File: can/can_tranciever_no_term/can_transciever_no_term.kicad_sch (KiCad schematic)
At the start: 6 parts, among them U5 TCAN3403DRQ1

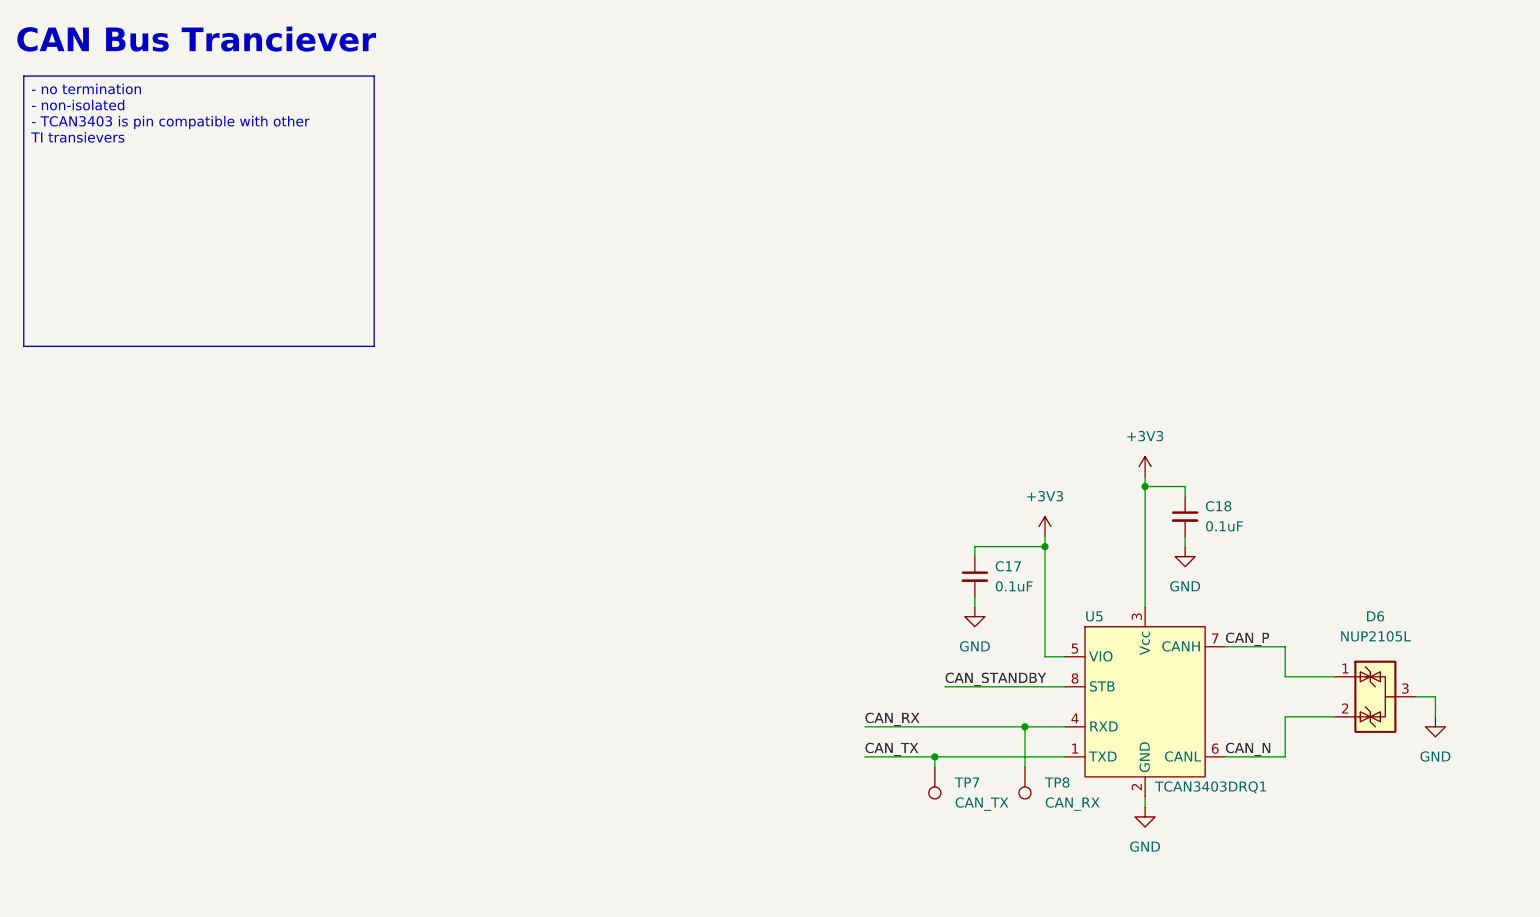
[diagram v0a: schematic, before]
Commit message: added hierarchical labels
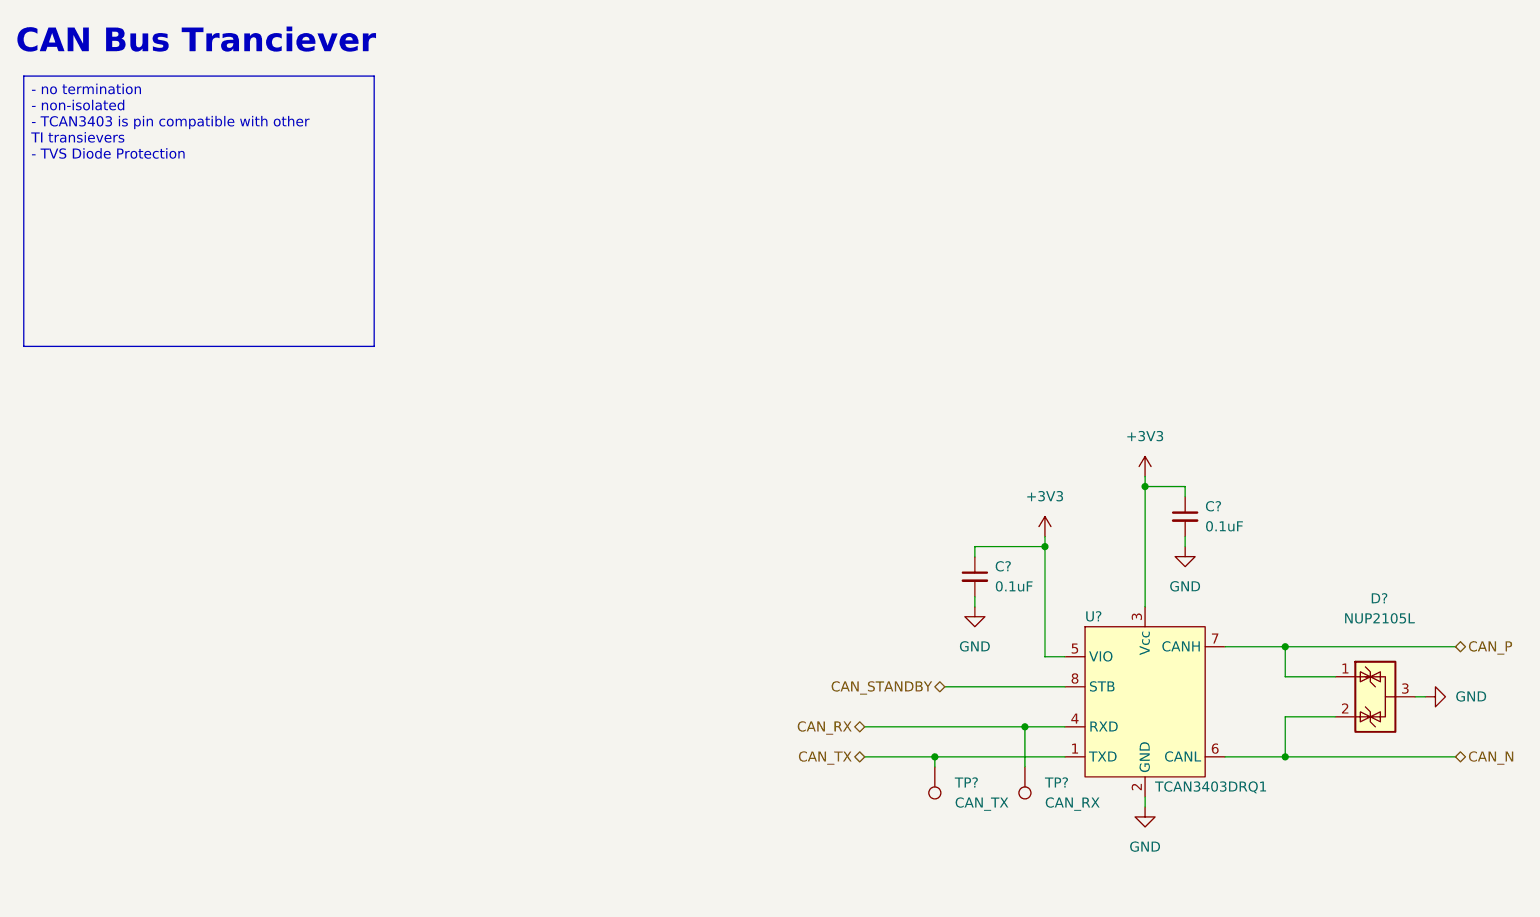
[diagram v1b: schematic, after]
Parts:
- renumbered C17 to C?, C18 to C?, D6 to D?, TP8 to TP?, TP7 to TP?, U5 to U?
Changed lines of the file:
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@@
 		)
 	)
-	(text_box "- no termination\n- non-isolated\n- TCAN3403 is pin compatible with other TI transievers"
+	(text_box "- no termination\n- non-isolated\n- TCAN3403 is pin compatible with other TI transievers\n- TVS Diode Protection"
 		(exclude_from_sim no)
 		(at 15.24 22.86 0)
@@
 	)
 	(junction
+		(at 175.26 109.22)
+		(diameter 0)
+		(color 0 0 0 0)
+	)
+	(junction
 		(at 144.78 82.55)
+		(diameter 0)
+		(color 0 0 0 0)
+	)
+	(junction
+		(at 175.26 95.25)
 		(diameter 0)
 		(color 0 0 0 0)
@@
 	(wire
 		(pts
+			(xy 175.26 109.22) (xy 196.85 109.22)
+		)
+		(stroke
+			(width 0)
+			(type default)
+		)
+	)
+	(wire
+		(pts
 			(xy 162.56 82.55) (xy 162.56 81.28)
 		)
@@
 	(wire
 		(pts
-			(xy 194.31 104.14) (xy 194.31 101.6)
-		)
-		(stroke
-			(width 0)
-			(type default)
-		)
-	)
-	(wire
-		(pts
 			(xy 175.26 95.25) (xy 175.26 99.06)
 		)
@@
 	(wire
 		(pts
-			(xy 194.31 101.6) (xy 191.77 101.6)
+			(xy 193.04 101.6) (xy 191.77 101.6)
 		)
 		(stroke
@@
 	(wire
 		(pts
+			(xy 175.26 95.25) (xy 196.85 95.25)
+		)
+		(stroke
+			(width 0)
+			(type default)
+		)
+	)
+	(wire
+		(pts
 			(xy 130.81 109.22) (xy 130.81 110.49)
 		)
@@
 		)
 	)
-	(label "CAN_P"
-		(at 167.64 95.25 0)
+	(hierarchical_label "CAN_P"
+		(shape bidirectional)
+		(at 196.85 95.25 0)
 		(effects
 			(font
 				(size 1.27 1.27)
 			)
-			(justify left bottom)
-		)
-	)
-	(label "CAN_N"
-		(at 167.64 109.22 0)
+			(justify left)
+		)
+	)
+	(hierarchical_label "CAN_N"
+		(shape bidirectional)
+		(at 196.85 109.22 0)
 		(effects
 			(font
 				(size 1.27 1.27)
 			)
-			(justify left bottom)
-		)
-	)
-	(label "CAN_STANDBY"
-		(at 132.08 100.33 0)
+			(justify left)
+		)
+	)
+	(hierarchical_label "CAN_TX"
+		(shape bidirectional)
+		(at 121.92 109.22 180)
 		(effects
 			(font
 				(size 1.27 1.27)
 			)
-			(justify left bottom)
-		)
-	)
-	(label "CAN_RX"
-		(at 121.92 105.41 0)
+			(justify right)
+		)
+	)
+	(hierarchical_label "CAN_STANDBY"
+		(shape bidirectional)
+		(at 132.08 100.33 180)
 		(effects
 			(font
 				(size 1.27 1.27)
 			)
-			(justify left bottom)
-		)
-	)
-	(label "CAN_TX"
-		(at 121.92 109.22 0)
+			(justify right)
+		)
+	)
+	(hierarchical_label "CAN_RX"
+		(shape bidirectional)
+		(at 121.92 105.41 180)
 		(effects
 			(font
 				(size 1.27 1.27)
 			)
-			(justify left bottom)
+			(justify right)
 		)
 	)
@@
 		(dnp no)
 		(fields_autoplaced yes)
-		(property "Reference" "TP8"
+		(property "Reference" "TP?"
 			(at 144.78 112.5219 0)
 			(effects
@@
 		)
 		(instances
+			(project "can_transciever_no_term"
+				(path "/7106a0b2-f612-48d7-957a-fac2f88be8f8"
+					(reference "TP?")
+					(unit 1)
+				)
+			)
 			(project "canbus_tire_temp_sensor"
 				(path "/e63e39d7-6ac0-4ffd-8aa3-1841a4541b55/5309e4c3-f3b7-4930-9c5f-4b2eb6027320"
@@
 		(dnp no)
 		(fields_autoplaced yes)
-		(property "Reference" "#PWR040"
+		(property "Reference" "#PWR?"
 			(at 162.56 88.9 0)
 			(effects
@@
 		)
 		(instances
+			(project "can_transciever_no_term"
+				(path "/7106a0b2-f612-48d7-957a-fac2f88be8f8"
+					(reference "#PWR?")
+					(unit 1)
+				)
+			)
 			(project "canbus_tire_temp_sensor"
 				(path "/e63e39d7-6ac0-4ffd-8aa3-1841a4541b55/5309e4c3-f3b7-4930-9c5f-4b2eb6027320"
@@
 		(dnp no)
 		(fields_autoplaced yes)
-		(property "Reference" "#PWR038"
+		(property "Reference" "#PWR?"
 			(at 157.48 77.47 0)
 			(effects
@@
 		)
 		(instances
+			(project "can_transciever_no_term"
+				(path "/7106a0b2-f612-48d7-957a-fac2f88be8f8"
+					(reference "#PWR?")
+					(unit 1)
+				)
+			)
 			(project "canbus_tire_temp_sensor"
 				(path "/e63e39d7-6ac0-4ffd-8aa3-1841a4541b55/5309e4c3-f3b7-4930-9c5f-4b2eb6027320"
@@
 	(symbol
 		(lib_id "power:GND")
-		(at 194.31 104.14 0)
+		(at 193.04 101.6 90)
 		(unit 1)
 		(exclude_from_sim no)
@@
 		(dnp no)
 		(fields_autoplaced yes)
-		(property "Reference" "#PWR041"
-			(at 194.31 110.49 0)
+		(property "Reference" "#PWR?"
+			(at 199.39 101.6 0)
 			(effects
 				(font
@@
 		)
 		(property "Value" "GND"
-			(at 194.31 109.22 0)
-			(effects
-				(font
-					(size 1.27 1.27)
-				)
+			(at 196.85 101.5999 90)
+			(effects
+				(font
+					(size 1.27 1.27)
+				)
+				(justify right)
 			)
 		)
 		(property "Footprint" ""
-			(at 194.31 104.14 0)
+			(at 193.04 101.6 0)
 			(effects
 				(font
@@
 		)
 		(property "Datasheet" ""
-			(at 194.31 104.14 0)
+			(at 193.04 101.6 0)
 			(effects
 				(font
@@
 		)
 		(property "Description" ""
-			(at 194.31 104.14 0)
+			(at 193.04 101.6 0)
 			(effects
 				(font
@@
 		)
 		(instances
+			(project "can_transciever_no_term"
+				(path "/7106a0b2-f612-48d7-957a-fac2f88be8f8"
+					(reference "#PWR?")
+					(unit 1)
+				)
+			)
 			(project "canbus_tire_temp_sensor"
 				(path "/e63e39d7-6ac0-4ffd-8aa3-1841a4541b55/5309e4c3-f3b7-4930-9c5f-4b2eb6027320"
@@
 		(on_board yes)
 		(dnp no)
-		(property "Reference" "U5"
+		(property "Reference" "U?"
 			(at 149.86 91.44 0)
 			(effects
@@
 		)
 		(instances
+			(project "can_transciever_no_term"
+				(path "/7106a0b2-f612-48d7-957a-fac2f88be8f8"
+					(reference "U?")
+					(unit 1)
+				)
+			)
 			(project "canbus_tire_temp_sensor"
 				(path "/e63e39d7-6ac0-4ffd-8aa3-1841a4541b55/5309e4c3-f3b7-4930-9c5f-4b2eb6027320"
@@
 		(dnp no)
 		(fields_autoplaced yes)
-		(property "Reference" "#PWR037"
+		(property "Reference" "#PWR?"
 			(at 144.78 85.09 0)
 			(effects
@@
 		)
 		(instances
+			(project "can_transciever_no_term"
+				(path "/7106a0b2-f612-48d7-957a-fac2f88be8f8"
+					(reference "#PWR?")
+					(unit 1)
+				)
+			)
 			(project "canbus_tire_temp_sensor"
 				(path "/e63e39d7-6ac0-4ffd-8aa3-1841a4541b55/5309e4c3-f3b7-4930-9c5f-4b2eb6027320"
@@
 		(dnp no)
 		(fields_autoplaced yes)
-		(property "Reference" "C17"
+		(property "Reference" "C?"
 			(at 138.43 85.0962 0)
 			(effects
@@
 		)
 		(instances
+			(project "can_transciever_no_term"
+				(path "/7106a0b2-f612-48d7-957a-fac2f88be8f8"
+					(reference "C?")
+					(unit 1)
+				)
+			)
 			(project "canbus_tire_temp_sensor"
 				(path "/e63e39d7-6ac0-4ffd-8aa3-1841a4541b55/5309e4c3-f3b7-4930-9c5f-4b2eb6027320"
@@
 		(dnp no)
 		(fields_autoplaced yes)
-		(property "Reference" "#PWR039"
+		(property "Reference" "#PWR?"
 			(at 157.48 121.92 0)
 			(effects
@@
 		)
 		(instances
+			(project "can_transciever_no_term"
+				(path "/7106a0b2-f612-48d7-957a-fac2f88be8f8"
+					(reference "#PWR?")
+					(unit 1)
+				)
+			)
 			(project "canbus_tire_temp_sensor"
 				(path "/e63e39d7-6ac0-4ffd-8aa3-1841a4541b55/5309e4c3-f3b7-4930-9c5f-4b2eb6027320"
@@
 		(dnp no)
 		(fields_autoplaced yes)
-		(property "Reference" "#PWR036"
+		(property "Reference" "#PWR?"
 			(at 135.89 96.52 0)
 			(effects
@@
 		)
 		(instances
+			(project "can_transciever_no_term"
+				(path "/7106a0b2-f612-48d7-957a-fac2f88be8f8"
+					(reference "#PWR?")
+					(unit 1)
+				)
+			)
 			(project "canbus_tire_temp_sensor"
 				(path "/e63e39d7-6ac0-4ffd-8aa3-1841a4541b55/5309e4c3-f3b7-4930-9c5f-4b2eb6027320"
@@
 		(dnp no)
 		(fields_autoplaced yes)
-		(property "Reference" "C18"
+		(property "Reference" "C?"
 			(at 165.1 77.4762 0)
 			(effects
@@
 		)
 		(instances
+			(project "can_transciever_no_term"
+				(path "/7106a0b2-f612-48d7-957a-fac2f88be8f8"
+					(reference "C?")
+					(unit 1)
+				)
+			)
 			(project "canbus_tire_temp_sensor"
 				(path "/e63e39d7-6ac0-4ffd-8aa3-1841a4541b55/5309e4c3-f3b7-4930-9c5f-4b2eb6027320"
@@
 		(on_board yes)
 		(dnp no)
-		(fields_autoplaced yes)
-		(property "Reference" "D6"
-			(at 186.69 91.44 90)
+		(property "Reference" "D?"
+			(at 187.198 89.154 90)
 			(effects
 				(font
@@
 		)
 		(property "Value" "NUP2105L"
-			(at 186.69 93.98 90)
+			(at 187.198 91.694 90)
 			(effects
 				(font
@@
 		)
 		(instances
+			(project "can_transciever_no_term"
+				(path "/7106a0b2-f612-48d7-957a-fac2f88be8f8"
+					(reference "D?")
+					(unit 1)
+				)
+			)
 			(project "canbus_tire_temp_sensor"
 				(path "/e63e39d7-6ac0-4ffd-8aa3-1841a4541b55/5309e4c3-f3b7-4930-9c5f-4b2eb6027320"
@@
 		(dnp no)
 		(fields_autoplaced yes)
-		(property "Reference" "TP7"
+		(property "Reference" "TP?"
 			(at 133.35 112.5219 0)
 			(effects
@@
 		)
 		(instances
+			(project "can_transciever_no_term"
+				(path "/7106a0b2-f612-48d7-957a-fac2f88be8f8"
+					(reference "TP?")
+					(unit 1)
+				)
+			)
 			(project "canbus_tire_temp_sensor"
 				(path "/e63e39d7-6ac0-4ffd-8aa3-1841a4541b55/5309e4c3-f3b7-4930-9c5f-4b2eb6027320"
@@
 		)
 	)
+	(sheet_instances
+		(path "/"
+			(page "1")
+		)
+	)
+	(embedded_fonts no)
 )

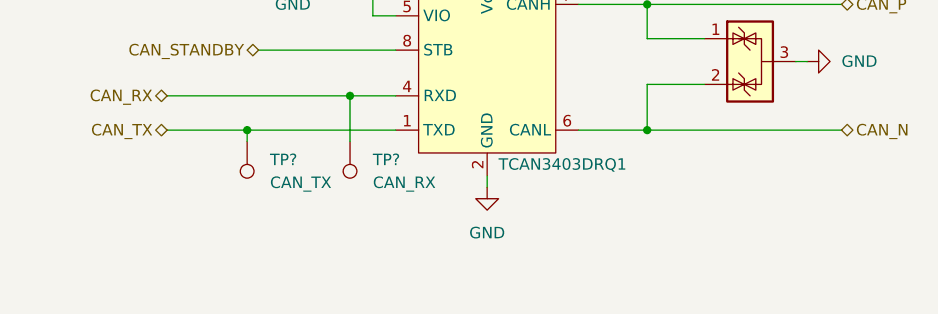
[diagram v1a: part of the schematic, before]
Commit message: Updated STM32 with different VCC symbol
- Added more integration details
- Added note regarding TCAN compatability to can tranciever schematic
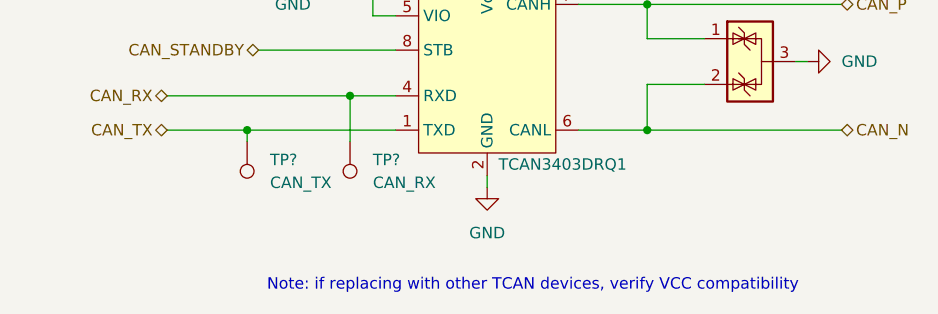
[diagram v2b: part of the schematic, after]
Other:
- note added: "Note: if replacing with other TCAN devices, verify VCC compatibility"
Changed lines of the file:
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@@
 	(generator_version "9.0")
 	(paper "A4")
+	(text "Note: if replacing with other TCAN devices, verify VCC compatibility "
+		(exclude_from_sim no)
+		(at 162.56 126.492 0)
+		(effects
+			(font
+				(size 1.27 1.27)
+			)
+		)
+	)
 	(text "CAN Bus Tranciever"
 		(exclude_from_sim no)
